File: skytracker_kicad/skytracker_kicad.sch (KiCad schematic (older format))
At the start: 21 parts, among them M1 28BYJ-48, SW1 HOME_DETECT, SW2 LIM_DETECT, SW3 STATE_SELECT, U1 ULN2003A

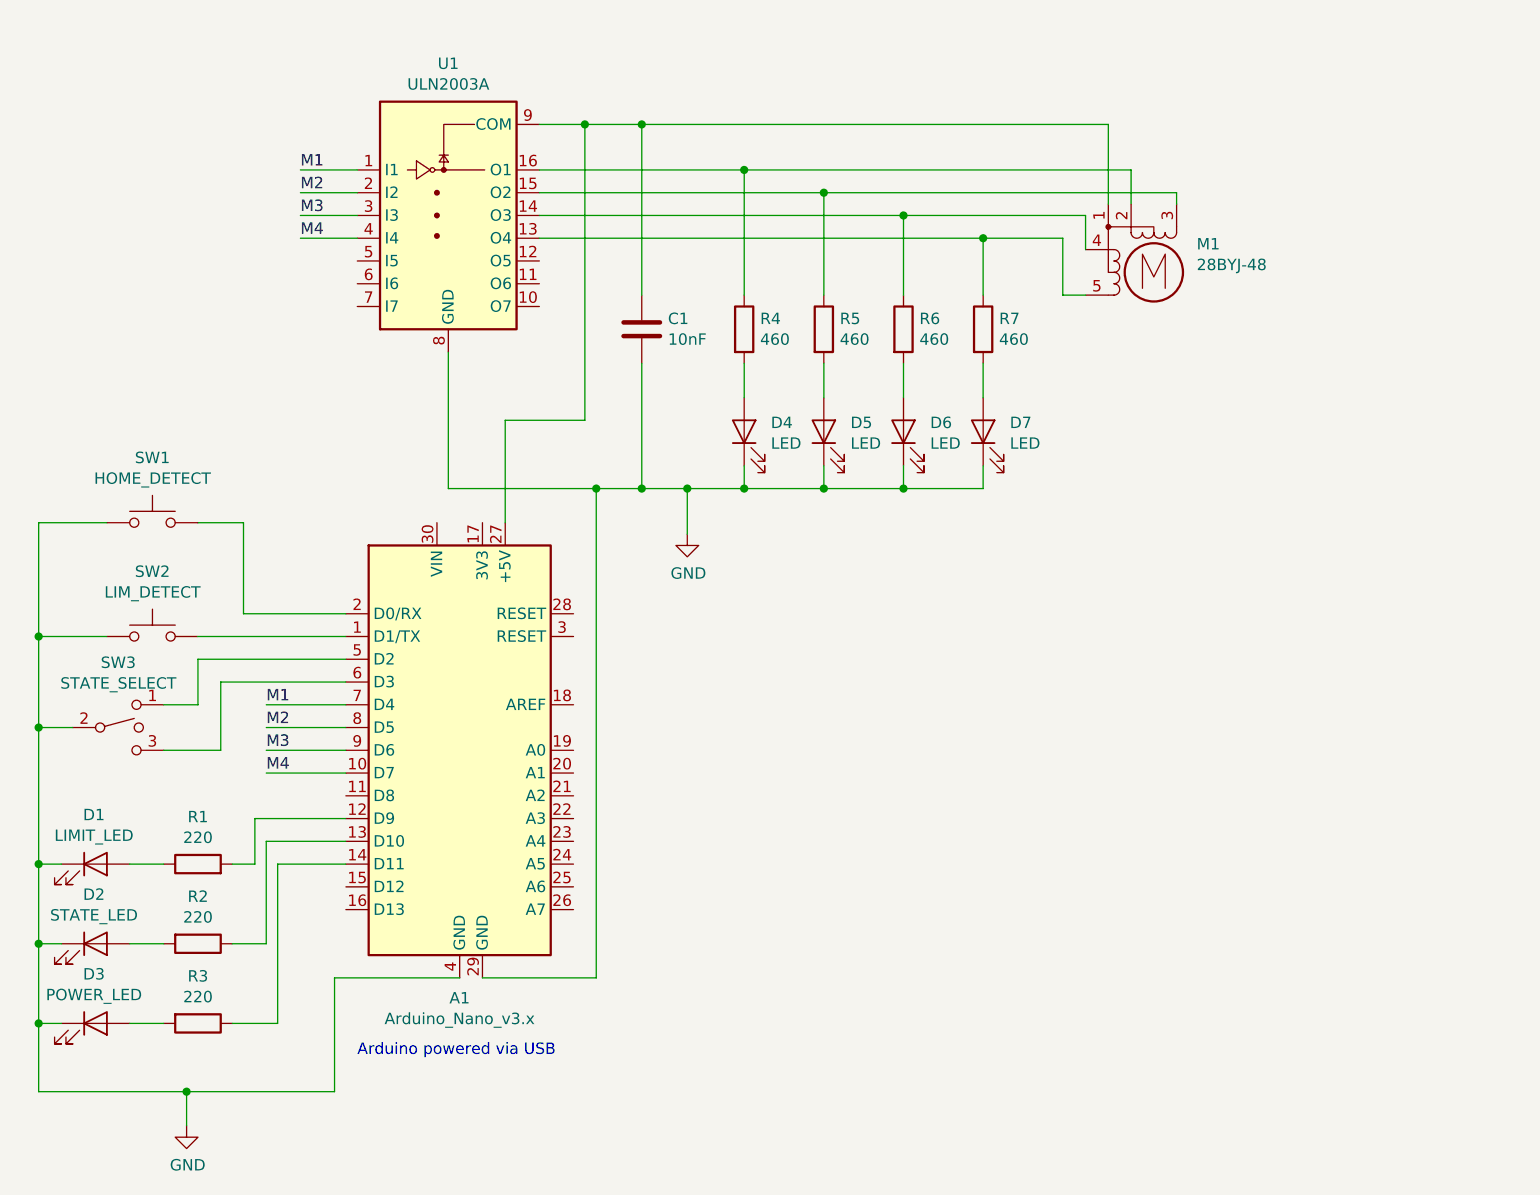
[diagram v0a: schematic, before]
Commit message: unipolar stepper
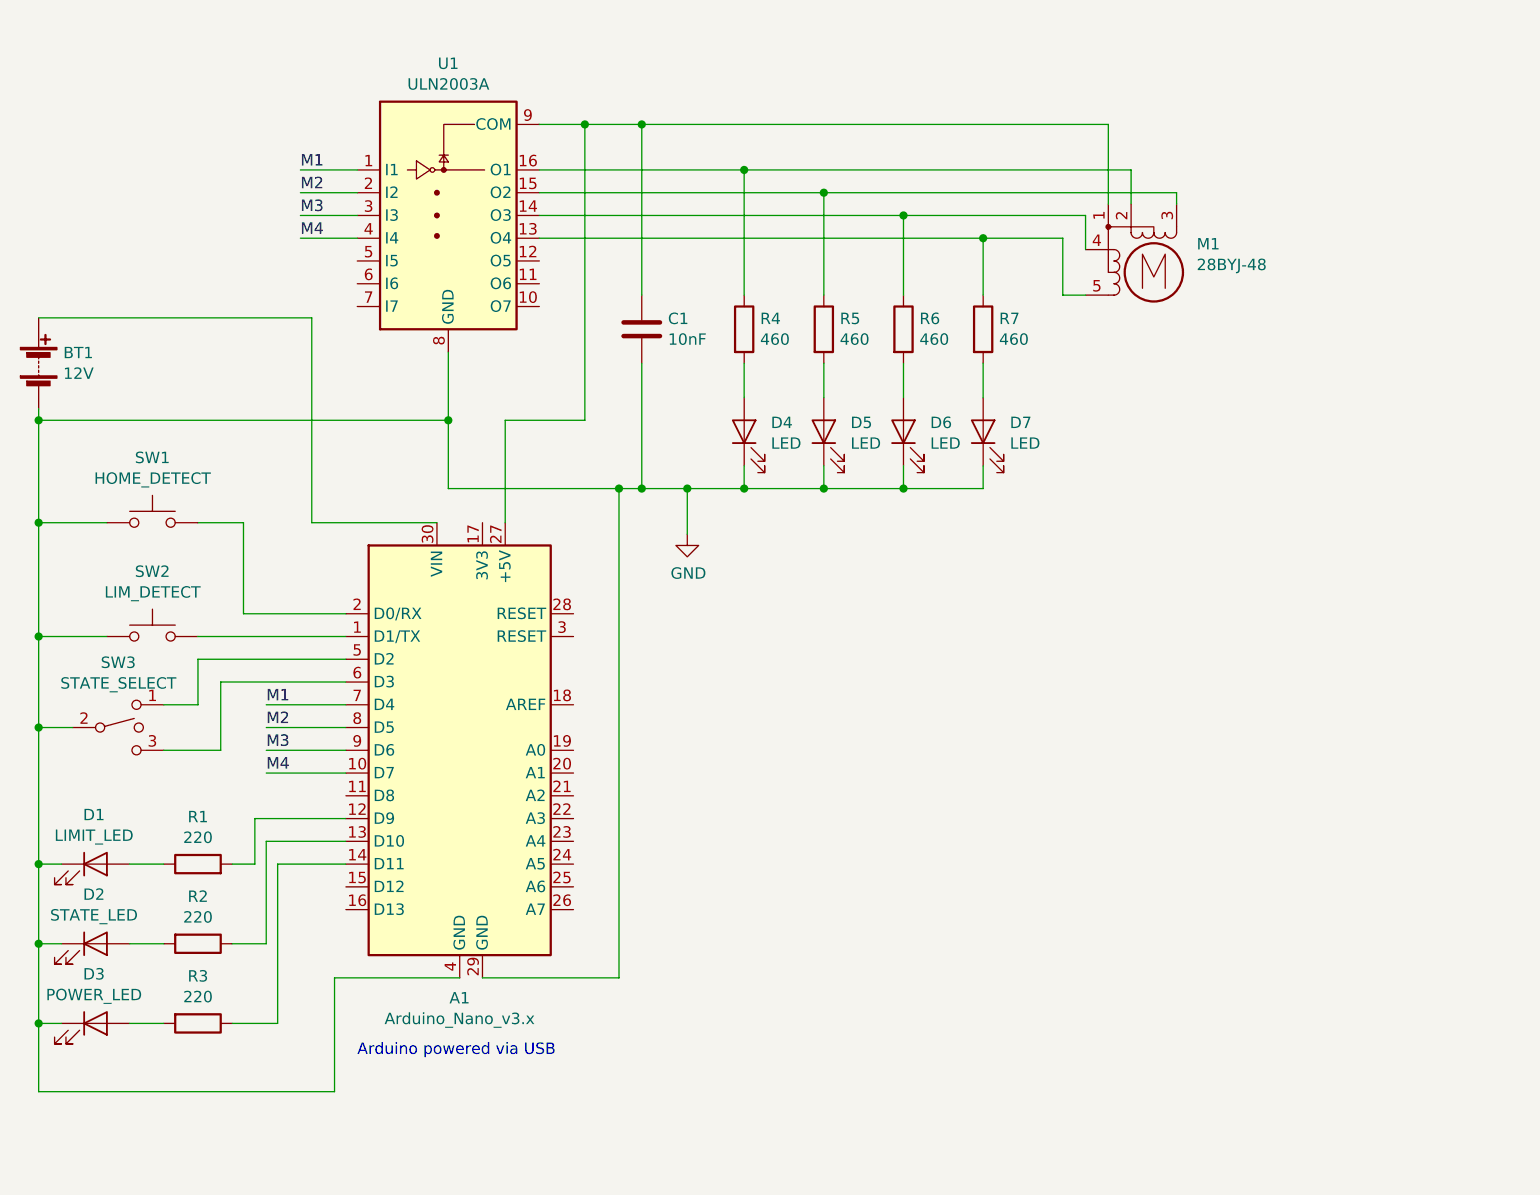
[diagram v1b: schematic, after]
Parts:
- added BT1: 12V, symbol Device:Battery
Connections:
- net GND: now also BT1.2 (-)
- net at A1.30 (VIN): now also BT1.1 (+)
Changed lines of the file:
@@
 	3850 4000 3550 4000
 Wire Wire Line
-	5500 5500 6000 5500
-Wire Wire Line
-	6000 5500 6000 3350
+	5500 5500 6100 5500
+Wire Wire Line
+	6100 5500 6100 3350
 $Comp
 L Transistor_Array:ULN2003A U1
@@
 	4700 2250 4950 2250
 Wire Wire Line
-	6000 3350 5350 3350
-Wire Wire Line
-	5350 3350 5350 2750
+	6100 3350 5350 3350
 Wire Wire Line
 	5600 3500 5600 3050
@@
 	6200 2800 6200 3350
 Wire Wire Line
-	6200 3350 6000 3350
-Connection ~ 6000 3350
+	6200 3350 6100 3350
+Connection ~ 6100 3350
 $Comp
 L Motor:Stepper_Motor_unipolar_5pin M1
@@
 Wire Wire Line
 	4850 5500 5400 5500
-Wire Wire Line
-	3550 6000 4200 6000
-$Comp
-L power:GND #PWR?
-U 1 1 5DAEAA02
-P 4200 6150
-F 0 "#PWR?" H 4200 5900 50  0001 C CNN
-F 1 "GND" H 4205 5977 50  0000 C CNN
-F 2 "" H 4200 6150 50  0001 C CNN
-F 3 "" H 4200 6150 50  0001 C CNN
-	1    4200 6150
-	1    0    0    -1
-$EndComp
-Wire Wire Line
-	4200 6150 4200 6000
-Connection ~ 4200 6000
-Wire Wire Line
-	4200 6000 4850 6000
-$Comp
-L power:GND #PWR?
+$Comp
+L power:GND #PWR01
 U 1 1 5DAEDE1E
 P 6400 3550
-F 0 "#PWR?" H 6400 3300 50  0001 C CNN
+F 0 "#PWR01" H 6400 3300 50  0001 C CNN
 F 1 "GND" H 6405 3377 50  0000 C CNN
 F 2 "" H 6400 3550 50  0001 C CNN
@@
 Wire Wire Line
 	4350 4500 4100 4500
+Wire Wire Line
+	4750 3500 5300 3500
+$Comp
+L Device:Battery BT1
+U 1 1 5DB5A285
+P 3550 2800
+F 0 "BT1" H 3658 2846 50  0000 L CNN
+F 1 "12V" H 3658 2755 50  0000 L CNN
+F 2 "" V 3550 2860 50  0001 C CNN
+F 3 "~" V 3550 2860 50  0001 C CNN
+	1    3550 2800
+	1    0    0    -1
+$EndComp
+Wire Wire Line
+	3550 6000 4850 6000
+Wire Wire Line
+	3550 3000 3550 3050
+Connection ~ 3550 3500
+Wire Wire Line
+	3550 2600 4750 2600
+Wire Wire Line
+	4750 2600 4750 3500
+Wire Wire Line
+	5350 2750 5350 3050
+Wire Wire Line
+	3550 3050 5350 3050
+Connection ~ 3550 3050
+Wire Wire Line
+	3550 3050 3550 3500
+Connection ~ 5350 3050
+Wire Wire Line
+	5350 3050 5350 3350
 $EndSCHEMATC

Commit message: 12V to motor
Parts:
- removed M1: 28BYJ-48, symbol Motor:Stepper_Motor_unipolar_5pin
- added M1: Stepper_Motor_bipolar, symbol Motor:Stepper_Motor_bipolar
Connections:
- net at C1.1, U1.9 (COM): now also A1.30 (VIN), BT1.1 (+); no longer A1.27 (+5V)
- net at R7.1, U1.13 (O4): now also M1.4
- net at R6.1, U1.14 (O3): now also M1.3
- net at R5.1, U1.15 (O2): now also M1.2 (-)
- net at R4.1, U1.16 (O1): now also M1.1
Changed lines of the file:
@@
 Wire Wire Line
 	6100 3350 5350 3350
-Wire Wire Line
-	5600 3500 5600 3050
-Wire Wire Line
-	5600 3050 5950 3050
-Wire Wire Line
-	5950 3050 5950 1750
-Wire Wire Line
-	5950 1750 5750 1750
 $Comp
 L Device:C C1
@@
 $EndComp
 Wire Wire Line
-	5950 1750 6200 1750
-Connection ~ 5950 1750
-Wire Wire Line
 	6200 2800 6200 3350
 Wire Wire Line
 	6200 3350 6100 3350
 Connection ~ 6100 3350
-$Comp
-L Motor:Stepper_Motor_unipolar_5pin M1
-U 1 1 5DB117CB
-P 8450 2400
-F 0 "M1" H 8638 2524 50  0000 L CNN
-F 1 "28BYJ-48" H 8638 2433 50  0000 L CNN
-F 2 "" H 8460 2390 50  0001 C CNN
-F 3 "http://www.infineon.com/dgdl/Application-Note-TLE8110EE_driving_UniPolarStepperMotor_V1.1.pdf?fileId=db3a30431be39b97011be5d0aa0a00b0" H 8460 2390 50  0001 C CNN
-	1    8450 2400
-	1    0    0    -1
-$EndComp
-Wire Wire Line
-	8250 2100 8250 1750
 Wire Wire Line
 	6200 1750 6200 2500
 Wire Wire Line
-	8350 1950 8350 2100
-Wire Wire Line
-	8550 2050 8550 2100
-Wire Wire Line
-	8150 2150 8150 2300
-Wire Wire Line
-	8050 2250 8050 2500
-Wire Wire Line
-	8050 2500 8150 2500
+	8400 2250 8400 2350
 Wire Wire Line
 	5750 1950 6650 1950
@@
 Wire Wire Line
 	5750 2250 7700 2250
-Wire Wire Line
-	6200 1750 8250 1750
-Connection ~ 6200 1750
 $Comp
 L Device:R R7
@@
 Connection ~ 6650 1950
 Wire Wire Line
-	6650 1950 8350 1950
+	6650 1950 8750 1950
 Wire Wire Line
 	7000 2500 7000 2050
 Connection ~ 7000 2050
 Wire Wire Line
-	7000 2050 8550 2050
+	7000 2050 8400 2050
 Wire Wire Line
 	7350 2500 7350 2150
 Connection ~ 7350 2150
 Wire Wire Line
-	7350 2150 8150 2150
+	7350 2150 8550 2150
 Wire Wire Line
 	7700 2500 7700 2250
 Connection ~ 7700 2250
 Wire Wire Line
-	7700 2250 8050 2250
+	7700 2250 8400 2250
 $Comp
 L Device:LED D4
@@
 Wire Wire Line
 	5350 3050 5350 3350
+$Comp
+L Motor:Stepper_Motor_bipolar M1
+U 1 1 5DB847A9
+P 8850 2250
+F 0 "M1" H 9038 2374 50  0000 L CNN
+F 1 "Stepper_Motor_bipolar" H 9038 2283 50  0000 L CNN
+F 2 "" H 8860 2240 50  0001 C CNN
+F 3 "http://www.infineon.com/dgdl/Application-Note-TLE8110EE_driving_UniPolarStepperMotor_V1.1.pdf?fileId=db3a30431be39b97011be5d0aa0a00b0" H 8860 2240 50  0001 C CNN
+	1    8850 2250
+	1    0    0    -1
+$EndComp
+Wire Wire Line
+	8400 2050 8400 1850
+Wire Wire Line
+	8400 1850 8950 1850
+Wire Wire Line
+	8950 1850 8950 1950
+Wire Wire Line
+	8400 2350 8550 2350
+Wire Wire Line
+	5750 1750 6200 1750
+Wire Wire Line
+	3550 2600 3550 1300
+Wire Wire Line
+	3550 1300 6200 1300
+Wire Wire Line
+	6200 1300 6200 1750
+Connection ~ 3550 2600
+Connection ~ 6200 1750
 $EndSCHEMATC

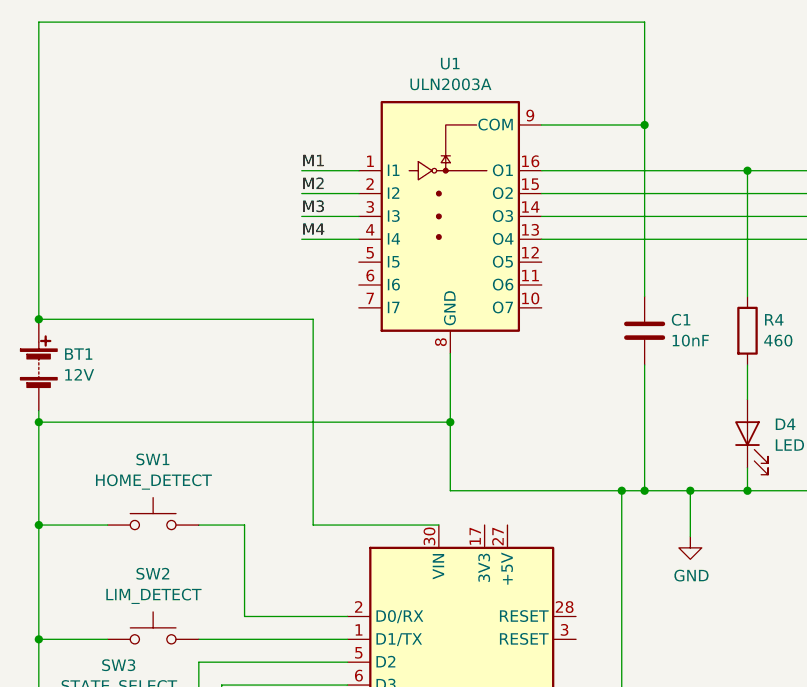
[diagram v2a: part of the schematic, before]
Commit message: add power switch
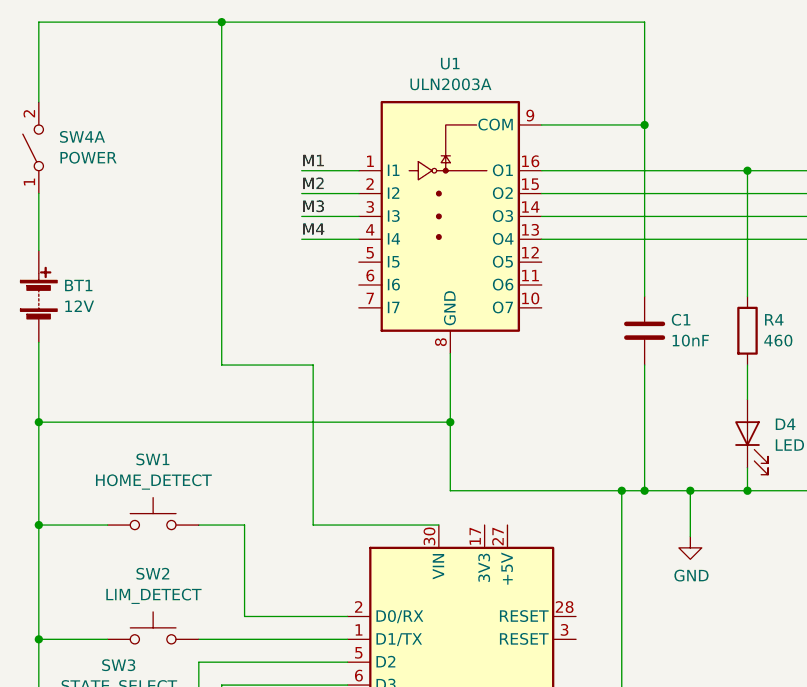
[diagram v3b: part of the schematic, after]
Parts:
- added SW4: POWER, symbol Switch:SW_DPST_x2
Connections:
- net at A1.30 (VIN), C1.1, U1.9 (COM): now also SW4.2 (B); no longer BT1.1 (+)
- new net: BT1.1 (+), SW4.1 (A)
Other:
- moved on the sheet: BT1
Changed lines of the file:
@@
 L Device:Battery BT1
 U 1 1 5DB5A285
-P 3550 2800
-F 0 "BT1" H 3658 2846 50  0000 L CNN
-F 1 "12V" H 3658 2755 50  0000 L CNN
-F 2 "" V 3550 2860 50  0001 C CNN
-F 3 "~" V 3550 2860 50  0001 C CNN
-	1    3550 2800
+P 3550 2500
+F 0 "BT1" H 3658 2546 50  0000 L CNN
+F 1 "12V" H 3658 2455 50  0000 L CNN
+F 2 "" V 3550 2560 50  0001 C CNN
+F 3 "~" V 3550 2560 50  0001 C CNN
+	1    3550 2500
 	1    0    0    -1
 $EndComp
@@
 	3550 6000 4850 6000
 Wire Wire Line
-	3550 3000 3550 3050
+	3550 2700 3550 3050
 Connection ~ 3550 3500
 Wire Wire Line
-	3550 2600 4750 2600
-Wire Wire Line
-	4750 2600 4750 3500
+	4750 2800 4750 3500
 Wire Wire Line
 	5350 2750 5350 3050
@@
 	5750 1750 6200 1750
 Wire Wire Line
-	3550 2600 3550 1300
-Wire Wire Line
-	3550 1300 6200 1300
+	3550 1300 4350 1300
 Wire Wire Line
 	6200 1300 6200 1750
-Connection ~ 3550 2600
 Connection ~ 6200 1750
+$Comp
+L Switch:SW_DPST_x2 SW4
+U 1 1 5DBA78CD
+P 3550 1850
+F 0 "SW4" V 3596 1762 50  0000 R CNN
+F 1 "POWER" V 3505 1762 50  0000 R CNN
+F 2 "" H 3550 1850 50  0001 C CNN
+F 3 "~" H 3550 1850 50  0001 C CNN
+	1    3550 1850
+	0    -1   -1   0
+$EndComp
+Wire Wire Line
+	3550 2050 3550 2300
+Wire Wire Line
+	3550 1650 3550 1300
+Wire Wire Line
+	4750 2800 4350 2800
+Wire Wire Line
+	4350 2800 4350 1300
+Connection ~ 4350 1300
+Wire Wire Line
+	4350 1300 6200 1300
 $EndSCHEMATC
